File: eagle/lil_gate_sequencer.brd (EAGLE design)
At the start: 106.9 x 81.8 mm, 69 parts, among them IC1 4093N, IC2 4017N, Q1 2N3904, Q2 2N3904

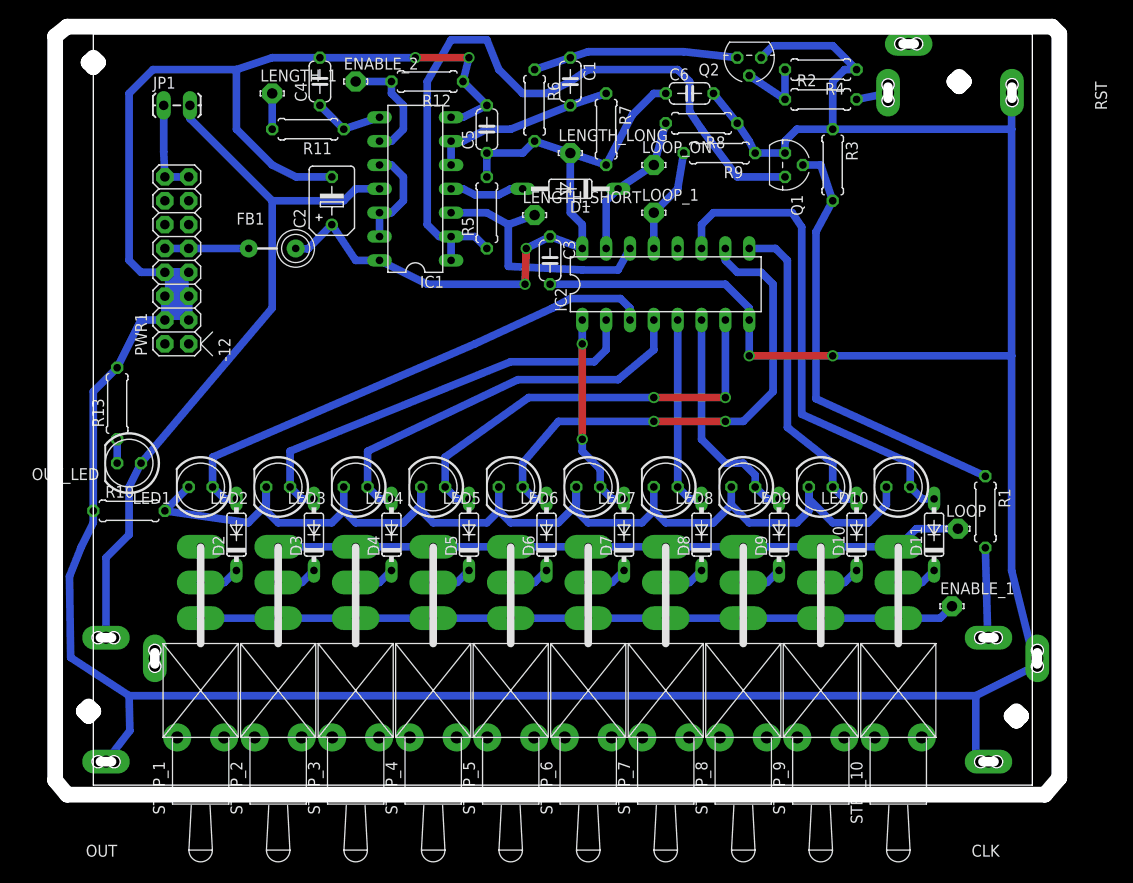
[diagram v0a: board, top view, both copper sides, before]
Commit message: normalled gate to reset and added reset to panel
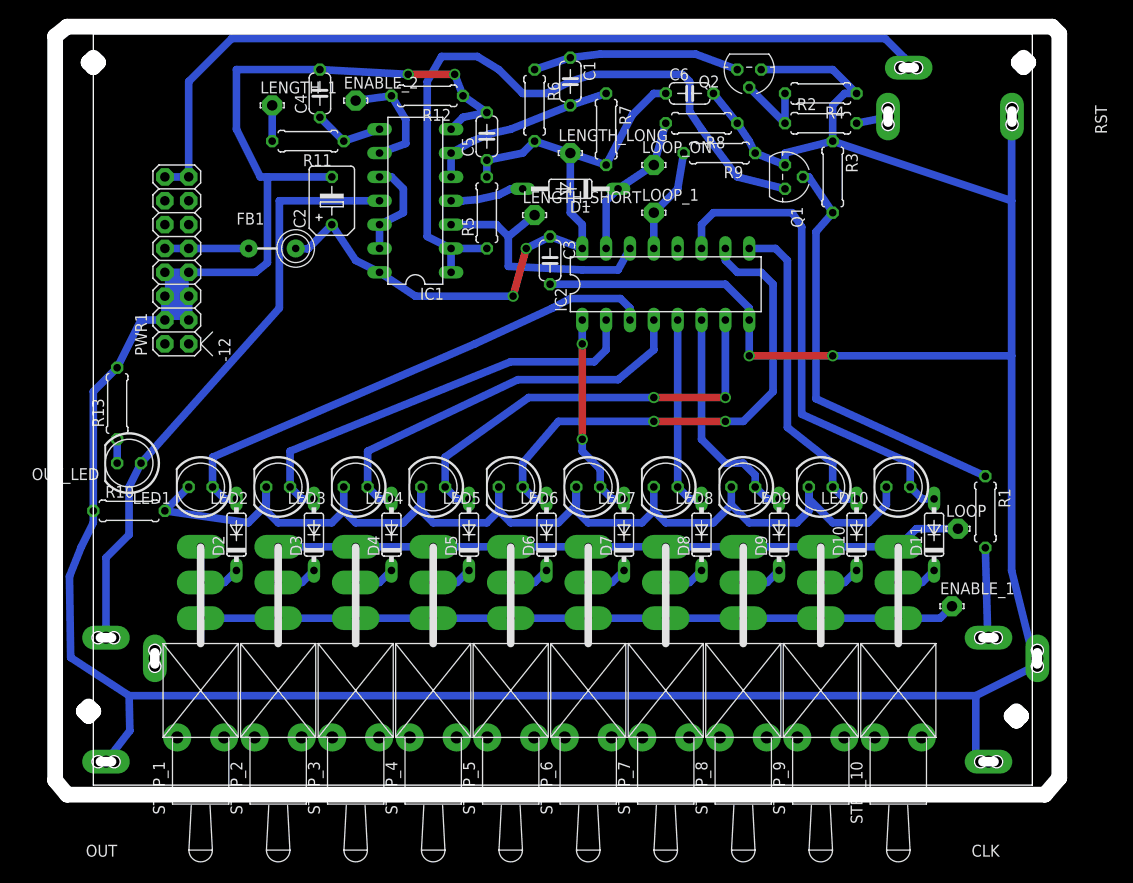
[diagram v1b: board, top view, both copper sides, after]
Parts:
- removed JP1: M02LOCK_LONGPADS, SparkFun-Connectors:1X02_LOCK_LONGPADS
- moved R2 2.54 mm to (77.5, 70.5)
- moved R4 2.54 mm to (77.5, 73.7)
- moved RST 2.54 mm to (100.3, 76.2)
- moved ENABLE_2 2.03 mm to (27.9, 72.9)
- moved R12 1.52 mm to (35.6, 73.4)
- moved C4 1.27 mm to (24.1, 73.7)
- moved Q1 1.27 mm to (73.7, 64.8)
- moved R3 1.27 mm to (78.7, 64.8)
- moved IC1 1.27 mm to (34.3, 62.2)
- moved LENGTH_1 1.27 mm to (19.1, 72.4)
- moved Q2 1.27 mm to (69.8, 76.2)
- moved R11 1.27 mm to (22.9, 68.6)
- moved C5 0.76 mm to (41.9, 69.1)
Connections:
- net N$39: now also RST.P$2; no longer JP1.1
- net N$6: no longer JP1.2
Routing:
- net N$39: track 10.2 -> 92.9 mm
- net GND: track 440.8 -> 417.2 mm
- net N$6: track 78.7 -> 64.1 mm
- net N$5: track 77.0 -> 74.4 mm
- net N$4: track 47.3 -> 45.5 mm
- net N$2: track 7.75 -> 8.56 mm
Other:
- outline, holes or cut-outs redrawn
